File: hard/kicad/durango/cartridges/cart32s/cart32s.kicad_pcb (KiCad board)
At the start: 2 copper layers, 49.5 x 48.3 mm, 7 parts, among them J1 EDGE CONNECTOR, U1 27C080, U2 CD4024

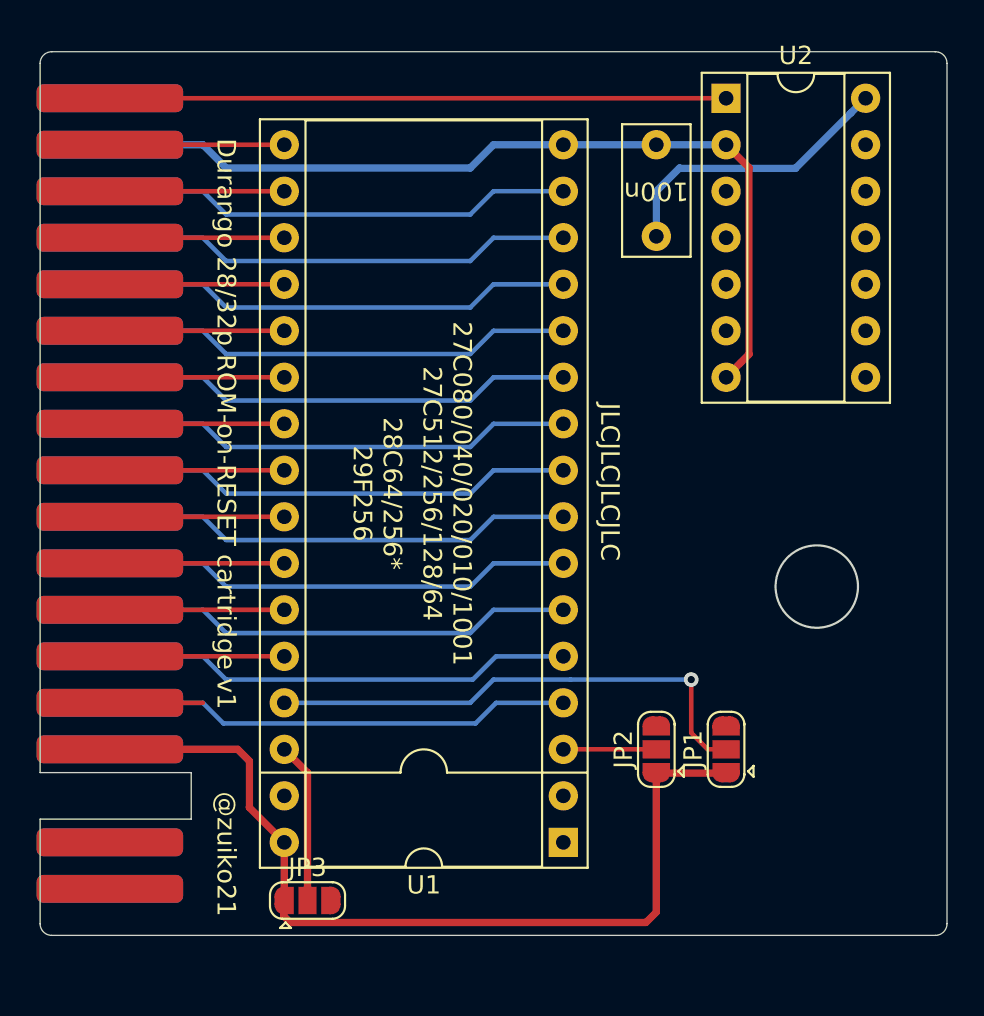
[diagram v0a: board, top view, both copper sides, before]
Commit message: mostly done 32p ROM-on-RESET
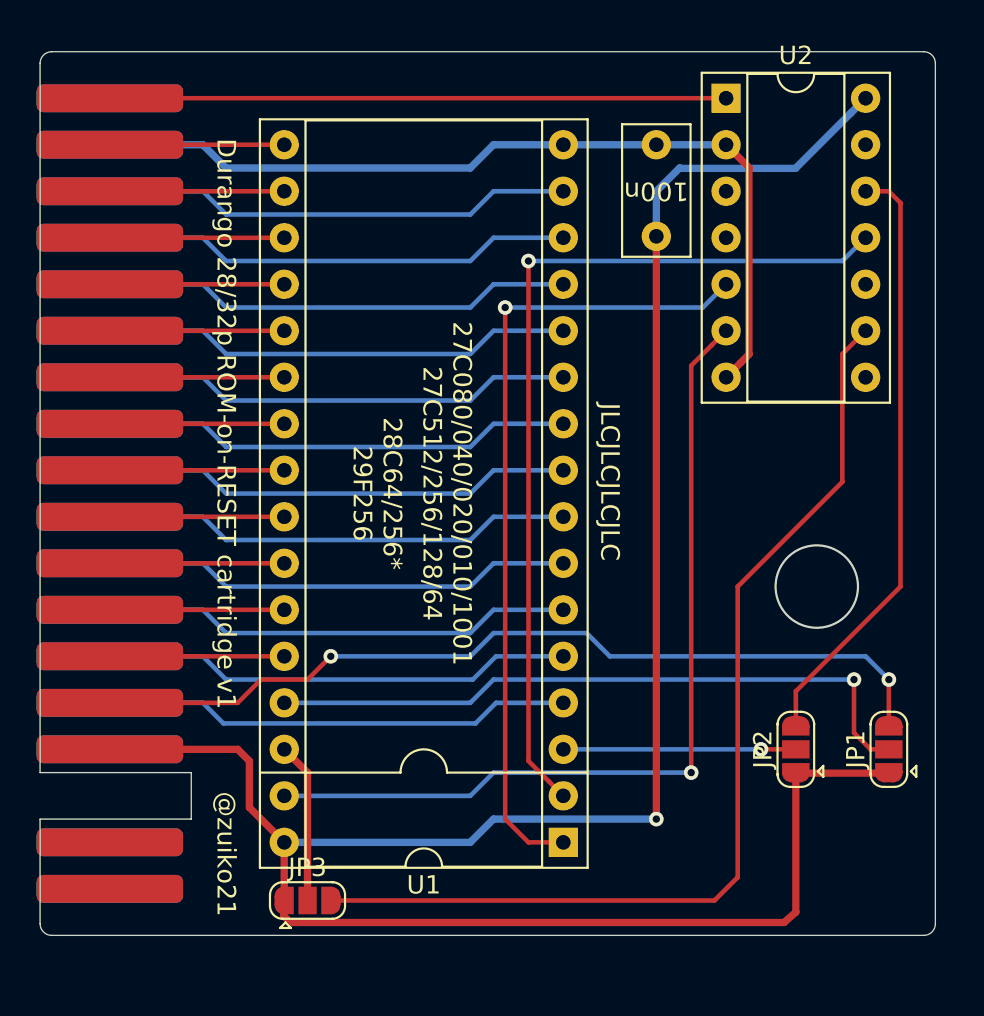
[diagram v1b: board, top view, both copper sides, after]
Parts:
- moved JP1 8.89 mm to (102.2, 66.0)
- moved JP2 7.62 mm to (97.2, 66.0)
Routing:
- net +5V: track 65.6 -> 127.1 mm, vias 0 -> 1
- net /ROM2: track 0.00 -> 55.5 mm
- net /ROM1: track 0.00 -> 48.9 mm, vias 0 -> 1
- net /ROM3: track 0.00 -> 47.7 mm, vias 0 -> 1
- net /ROM4: track 0.00 -> 44.2 mm, vias 0 -> 1
- net /A14: track 5.08 -> 47.7 mm, vias 0 -> 2
- net /ROM0: track 0.00 -> 33.1 mm
- net /P27: track 28.8 -> 37.7 mm
- net /P01: track 5.08 -> 12.7 mm, vias 0 -> 1
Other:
- board size 49.5 x 48.3 mm -> 48.9 x 48.3 mm

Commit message: add power planes and serigraphy to cart32s
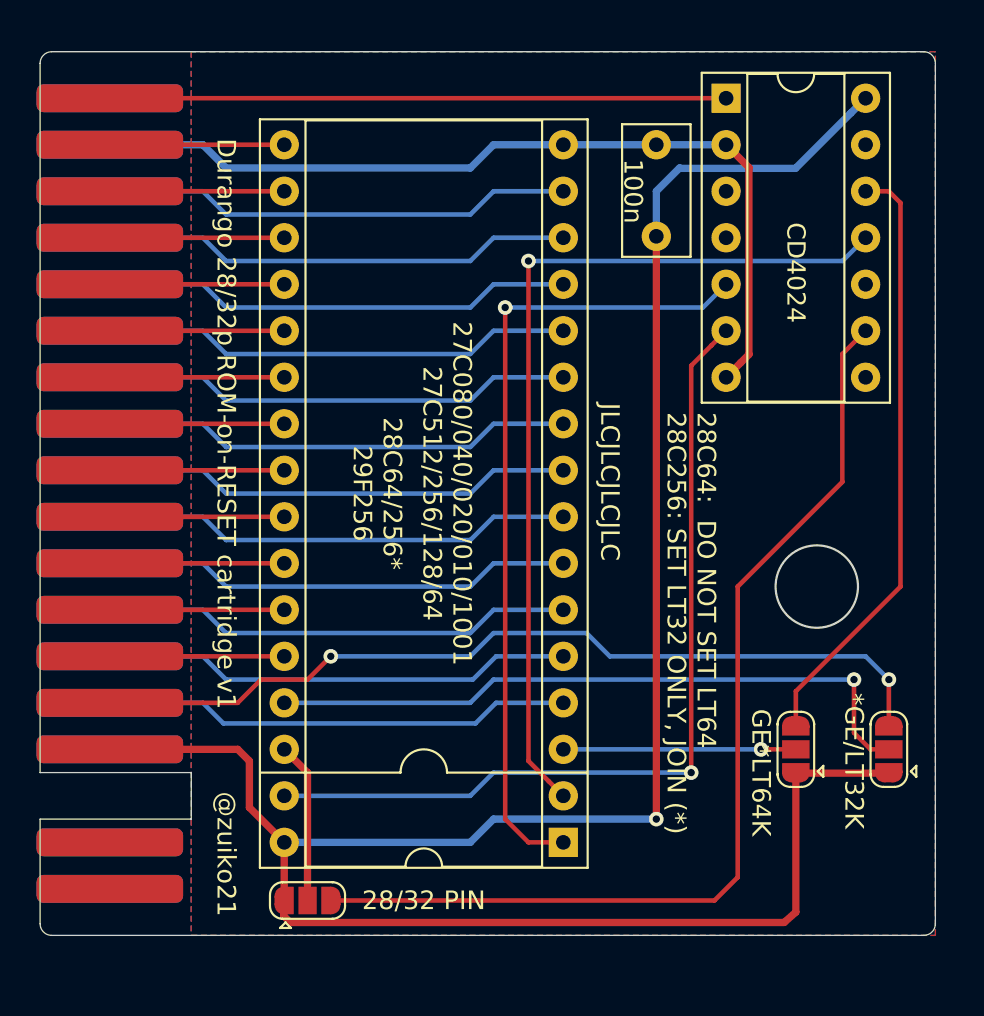
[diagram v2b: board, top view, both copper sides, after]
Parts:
- JP3: value 28/32P -> 28/32 PIN
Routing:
- added copper zone on F.Cu, net +5V
- added copper zone on B.Cu, net GND
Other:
- board text added: "28C64: DO NOT SET LT64 28C256: SET LT32 ONLY, JOIN (*)"
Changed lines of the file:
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@@
   (general
     (thickness 1.6)
-    (drawings 21)
+    (drawings 22)
     (tracks 167)
     (zones 0)
@@
     (descr "14-lead though-hole mounted DIP package, row spacing 7.62 mm (300 mils), Socket")
     (tags "THT DIP DIL PDIP 2.54mm 7.62mm 300mil Socket")
-    (fp_text reference U2 (at 3.81 -2.33) (layer F.SilkS)
-      (effects (font (size 1 1) (thickness 0.15)))
-    )
-    (fp_text value CD4024 (at 3.81 17.57) (layer F.Fab)
+    (fp_text reference U2 (at 3.81 0 270 unlocked) (layer B.SilkS)
+      (effects (font (size 1 1) (thickness 0.15)) (justify mirror))
+    )
+    (fp_text value CD4024 (at 3.81 9.525 270 unlocked) (layer F.SilkS)
       (effects (font (size 1 1) (thickness 0.15)))
     )
@@
     (descr "32-lead though-hole mounted DIP package, row spacing 15.24 mm (600 mils), Socket")
     (tags "THT DIP DIL PDIP 2.54mm 15.24mm 600mil Socket")
-    (fp_text reference U1 (at 7.62 -2.33) (layer F.SilkS)
-      (effects (font (size 1 1) (thickness 0.15)))
+    (fp_text reference U1 (at 7.62 0 270 unlocked) (layer B.SilkS)
+      (effects (font (size 1 1) (thickness 0.15)) (justify mirror))
     )
     (fp_text value 27C080 (at 7.62 40.43) (layer F.Fab)
@@
     (tags "solder jumper open")
     (attr virtual)
-    (fp_text reference JP3 (at 0 -1.8) (layer F.SilkS)
-      (effects (font (size 1 1) (thickness 0.15)))
-    )
-    (fp_text value 28/32P (at 0 1.9) (layer F.Fab)
-      (effects (font (size 1 1) (thickness 0.15)))
+    (fp_text reference JP3 (at 0 0) (layer B.SilkS)
+      (effects (font (size 1 1) (thickness 0.15)) (justify mirror))
+    )
+    (fp_text value "28/32 PIN" (at 6.35 0) (layer F.SilkS)
+      (effects (font (size 1.016 1.016) (thickness 0.15)))
     )
     (fp_arc (start -1.35 -0.3) (end -1.35 -1) (angle -90) (layer F.SilkS) (width 0.12))
@@
     (tags "solder jumper open")
     (attr virtual)
-    (fp_text reference JP2 (at 0 -1.8 90) (layer F.SilkS)
-      (effects (font (size 1 1) (thickness 0.15)))
-    )
-    (fp_text value GE*LT64K (at 0 1.9 90) (layer F.Fab)
-      (effects (font (size 1 1) (thickness 0.15)))
+    (fp_text reference JP2 (at 0 0 270 unlocked) (layer B.SilkS)
+      (effects (font (size 1 1) (thickness 0.15)) (justify mirror))
+    )
+    (fp_text value GE*LT64K (at -1.27 -1.905 270 unlocked) (layer F.SilkS)
+      (effects (font (size 1.016 1.016) (thickness 0.15)))
     )
     (fp_arc (start -1.35 -0.3) (end -1.35 -1) (angle -90) (layer F.SilkS) (width 0.12))
@@
     (tags "solder jumper open")
     (attr virtual)
-    (fp_text reference JP1 (at 0 -1.8 90) (layer F.SilkS)
-      (effects (font (size 1 1) (thickness 0.15)))
-    )
-    (fp_text value *GE/LT32K (at 0 1.9 90) (layer F.Fab)
-      (effects (font (size 1 1) (thickness 0.15)))
+    (fp_text reference JP1 (at 0 0 270 unlocked) (layer B.SilkS)
+      (effects (font (size 1 1) (thickness 0.15)) (justify mirror))
+    )
+    (fp_text value *GE/LT32K (at -0.635 -1.905 270 unlocked) (layer F.SilkS)
+      (effects (font (size 1.016 1.016) (thickness 0.15)))
     )
     (fp_arc (start -1.35 -0.3) (end -1.35 -1) (angle -90) (layer F.SilkS) (width 0.12))
@@
   (module edge_conn:Durango_ROM (layer F.Cu)
     (at 55.88 27.94 270)
-    (fp_text reference J1 (at 2.54 -8.89 unlocked) (layer B.SilkS)
+    (fp_text reference J1 (at 45.72 -9.525 270 unlocked) (layer B.SilkS)
       (effects (font (size 1.016 1.016) (thickness 0.16)) (justify mirror))
     )
@@
     (descr "C, Rect series, Radial, pin pitch=5.00mm, , length*width=7*3.5mm^2, Capacitor")
     (tags "C Rect series Radial pin pitch 5.00mm  length 7mm width 3.5mm Capacitor")
-    (fp_text reference C1 (at 2.5 0 90) (layer B.SilkS)
+    (fp_text reference C1 (at 2.5 0 270 unlocked) (layer B.SilkS)
       (effects (font (size 1 1) (thickness 0.16)) (justify mirror))
     )
-    (fp_text value 100n (at 2.54 0 180 unlocked) (layer F.SilkS)
+    (fp_text value 100n (at 2.54 1.27 270 unlocked) (layer F.SilkS)
       (effects (font (size 1.016 1.016) (thickness 0.16)))
     )
@@
       (rotate (xyz 0 0 0))
     )
+  )
+  (gr_text "28C64:  DO NOT SET LT64\n28C256: SET LT32 ONLY, JOIN (*)" (at 91.44 47.625 270) (layer F.SilkS)
+    (effects (font (size 1.016 1.016) (thickness 0.16)) (justify left))
   )
   (gr_circle (center 98.298 57.15) (end 100.548 57.15) (layer Edge.Cuts) (width 0.12))
@@
   (segment (start 81.28 41.91) (end 92.075 41.91) (width 0.25) (layer B.Cu) (net 36))
   (segment (start 92.075 41.91) (end 93.345 40.64) (width 0.25) (layer B.Cu) (net 36))
+  (zone (net 27) (net_name +5V) (layer F.Cu) (hatch edge 0.508)
+    (connect_pads (clearance 0.508))
+    (min_thickness 0.254)
+    (fill yes (arc_segments 32) (thermal_gap 0.508) (thermal_bridge_width 0.508))
+    (polygon
+      (pts
+        (xy 64.135 27.94) (xy 64.135 76.2) (xy 104.775 76.2) (xy 104.775 27.94)
+      )
+    )
+  )
+  (zone (net 1) (net_name GND) (layer B.Cu) (hatch edge 0.508)
+    (connect_pads (clearance 0.508))
+    (min_thickness 0.254)
+    (fill yes (arc_segments 32) (thermal_gap 0.508) (thermal_bridge_width 0.508))
+    (polygon
+      (pts
+        (xy 64.135 27.94) (xy 64.135 76.2) (xy 104.775 76.2) (xy 104.775 27.94)
+      )
+    )
+  )
 )
